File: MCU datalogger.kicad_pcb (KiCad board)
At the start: 2 copper layers, 29 parts, among them J1 Conn_01x04_Pin, J2 Conn_01x04_Pin, J3 Conn_01x09_Pin, J4 Conn_02x03_Odd_Even, U1 24LC1025, U2 24LC1025, U3 ATMEGA328P-AU, U4 DS1337S_, Y1 32.768 KHz, Y2 16MHz

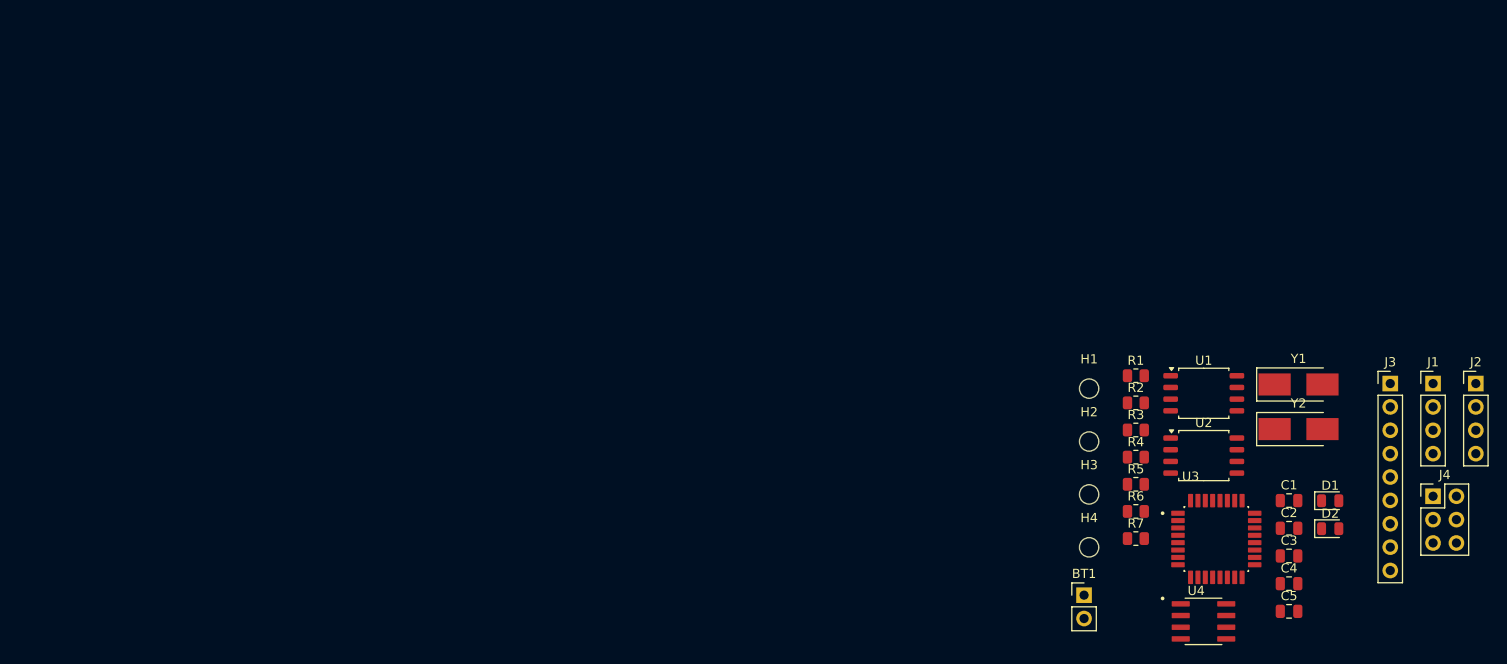
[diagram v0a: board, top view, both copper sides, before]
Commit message: complete placement of footprints
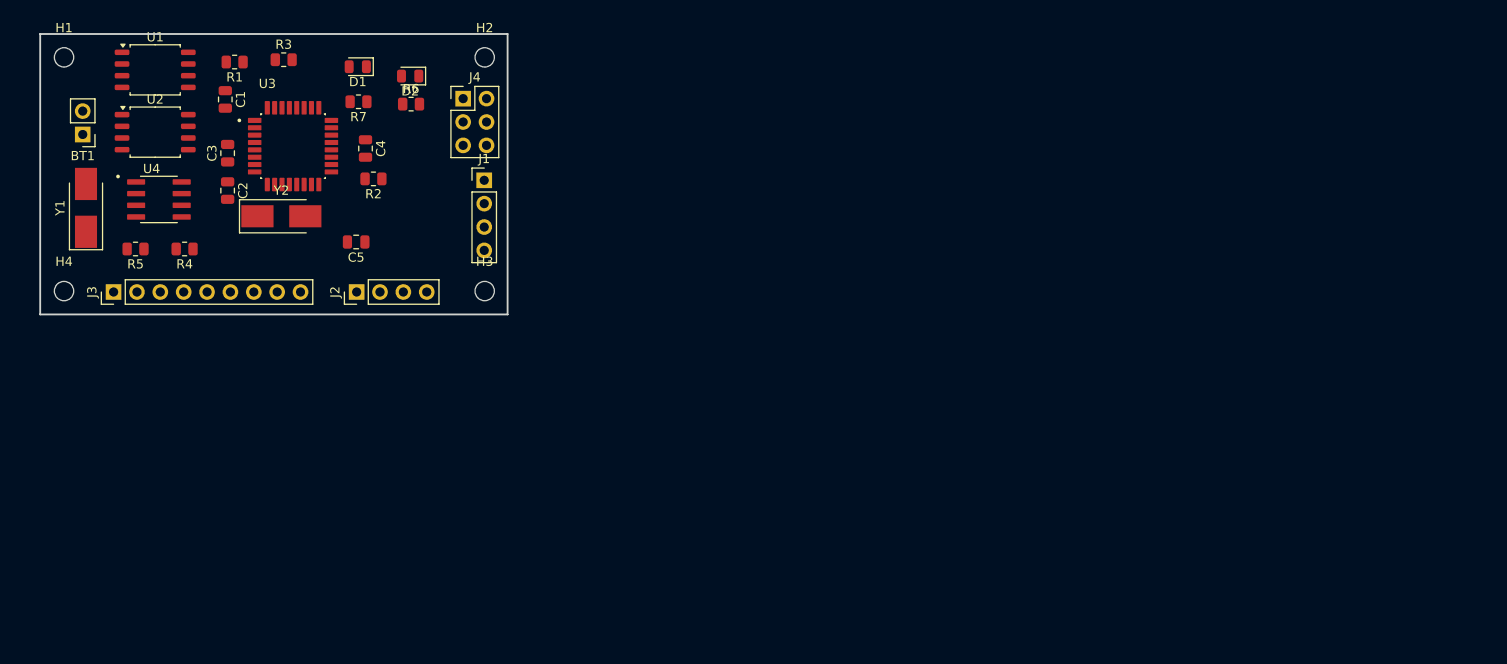
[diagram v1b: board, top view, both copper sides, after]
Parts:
- moved J3 139.1 mm to (104.4, 91.5), turned to 90 degrees
- moved Y1 133.2 mm to (101.4, 82.4), turned to 90 degrees
- moved C1 123.6 mm to (116.6, 70.6), turned to -90 degrees
- moved C3 123.4 mm to (116.8, 76.5), turned to 90 degrees
- moved U4 122.4 mm to (109.4, 81.5)
- moved J2 122.0 mm to (130.9, 91.5), turned to 90 degrees
- moved C2 121.1 mm to (116.8, 80.5), turned to -90 degrees
- moved BT1 119.8 mm to (101.1, 74.4), turned to 180 degrees
- moved U1 119.3 mm to (109.0, 67.4)
- moved U2 119.3 mm to (109.0, 74.2)
- moved H1 117.1 mm to (99.1, 66.0)
- moved D1 115.7 mm to (131.0, 67.1), turned to 180 degrees
- moved H4 114.8 mm to (99.1, 91.4)
- moved J4 113.9 mm to (142.4, 70.5)
- moved Y2 112.9 mm to (122.7, 83.3)
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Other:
- board outline added: 50.8 x 30.5 mm

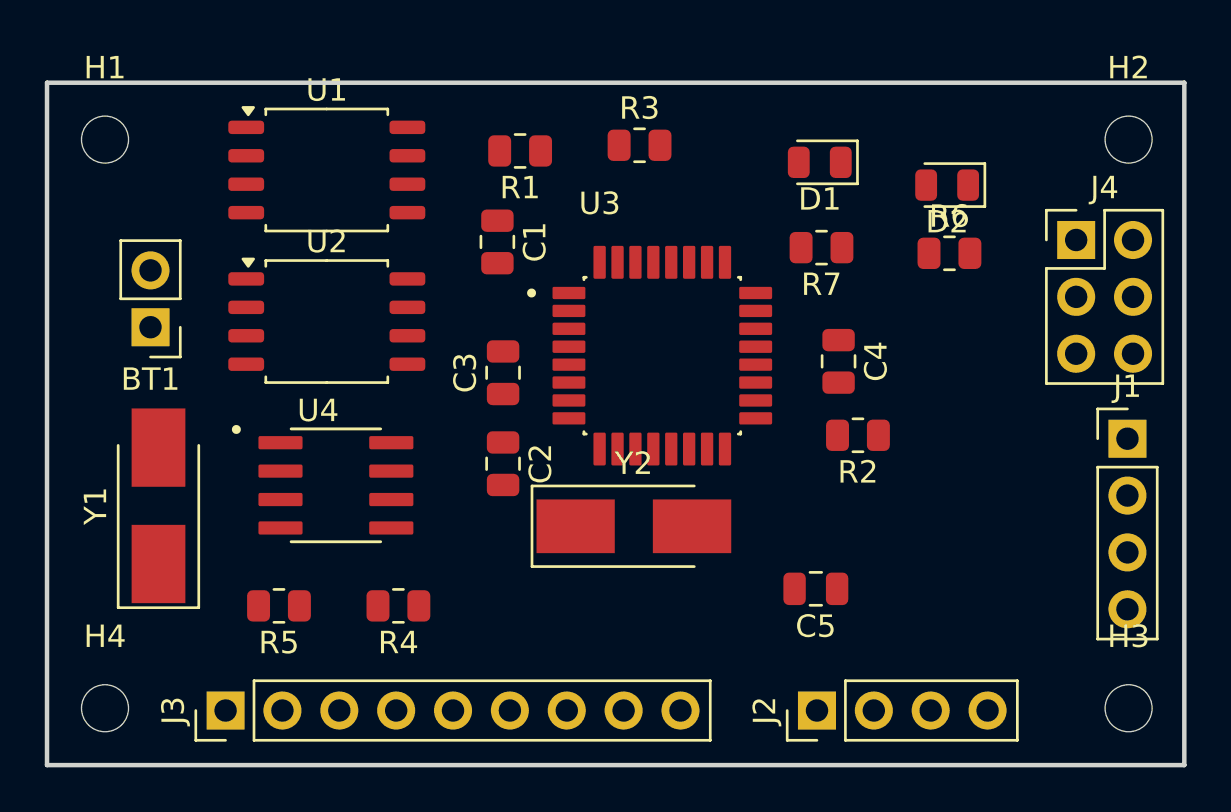
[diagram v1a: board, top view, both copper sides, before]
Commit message: routing expect gnd and vcc
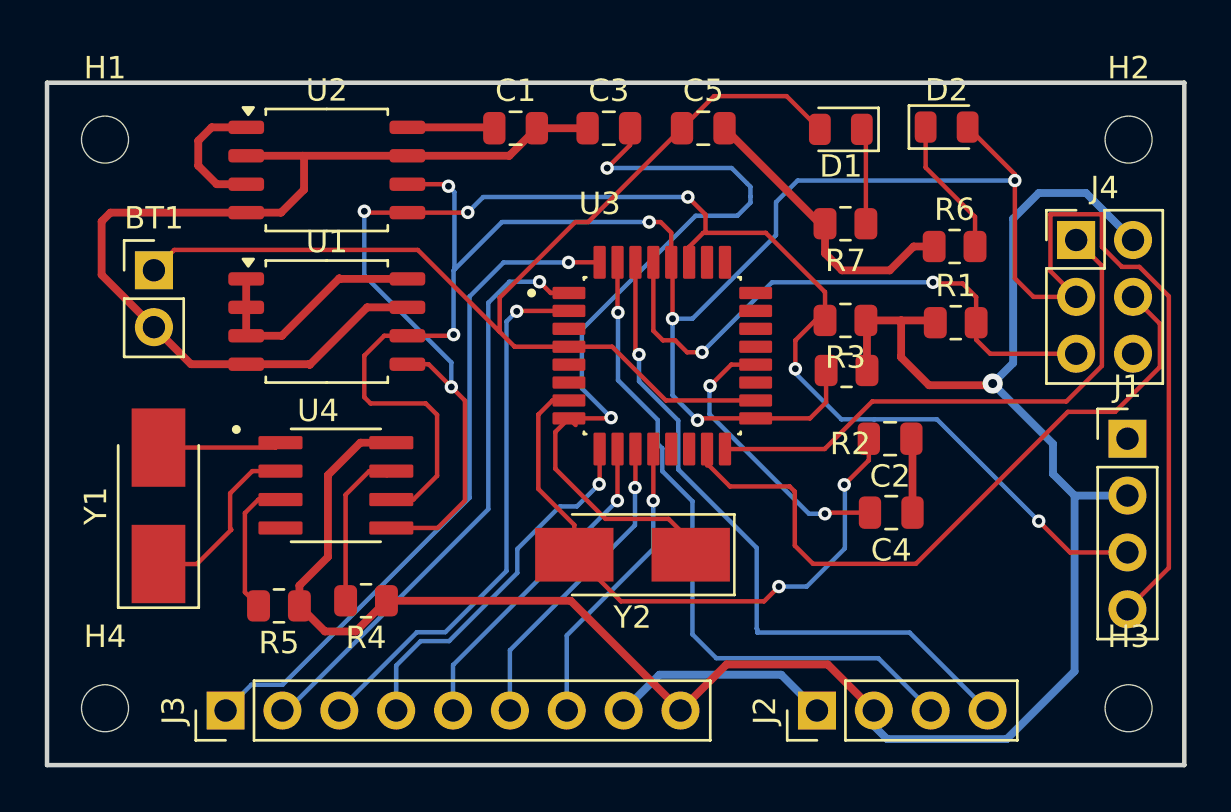
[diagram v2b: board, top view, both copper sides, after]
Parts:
- moved C5 21.2 mm to (125.8, 65.5), turned to 0 degrees
- moved R1 20.9 mm to (137.1, 74.2), turned to 0 degrees
- moved C2 17.3 mm to (134.1, 79.4), turned to 180 degrees
- moved R3 12.1 mm to (132.1, 74.1), turned to 180 degrees
- moved C3 11.9 mm to (121.6, 65.5), turned to 0 degrees
- moved C4 7.15 mm to (134.2, 82.7), turned to 180 degrees
- moved U1 6.77 mm to (109.0, 74.2)
- moved U2 6.77 mm to (109.0, 67.4)
- moved C1 5.14 mm to (117.4, 65.5), turned to 0 degrees
- moved R2 2.94 mm to (132.2, 76.4)
- moved D2 2.59 mm to (136.7, 65.5), turned to 0 degrees
- moved BT1 2.55 mm to (101.2, 71.9), turned to 0 degrees
- moved D1 1.75 mm to (131.9, 65.6)
- moved R7 1.51 mm to (132.1, 69.8)
- moved R4 1.46 mm to (110.7, 86.6)
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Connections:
- J2 pad 3: /RX -> /TX
- J2 pad 4: /TX -> /RX
- J4 pad 1: /MOSI -> /MISO
- J4 pad 4: /MISO -> /MOSI
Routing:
- net /VCC: track 0.00 -> 114.9 mm, vias 0 -> 1
- net /SCK: track 0.00 -> 106.7 mm, vias 0 -> 6
- net GND: track 0.00 -> 72.2 mm
- net /SDA: track 0.00 -> 68.4 mm, vias 0 -> 6
- net Net-(BT1-+): track 0.00 -> 50.2 mm
- net Net-(U3-PB7): track 0.00 -> 36.8 mm, vias 0 -> 2
- net /MOSI: track 0.00 -> 32.1 mm
- net /RX: track 0.00 -> 30.5 mm, vias 0 -> 1
- net /D2: track 0.00 -> 30.3 mm, vias 0 -> 1
- net /TX: track 0.00 -> 30.1 mm, vias 0 -> 1
- net Net-(U3-PB6): track 0.00 -> 27.8 mm, vias 0 -> 2
- net /D3: track 0.00 -> 26.3 mm, vias 0 -> 1
- net /RST: track 0.00 -> 26.1 mm, vias 0 -> 2
- net /MISO: track 0.00 -> 24.5 mm
- net /D4: track 0.00 -> 24.2 mm, vias 0 -> 1
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
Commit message: routing complete
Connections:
- BT1 pad 1: Net-(BT1-+) -> /VCC
- C5 pad 1: Net-(BT1-+) -> /VCC
- D1 pad 2: Net-(BT1-+) -> /VCC
- U3 pad 18: Net-(BT1-+) -> /VCC
- U3 pad 4: Net-(BT1-+) -> /VCC
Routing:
- net /VCC: track 114.9 -> 166.2 mm, vias 1 -> 3
- net Net-(BT1-+): track 50.2 -> 0.00 mm
- net GND: track 72.2 -> 114.6 mm, vias 0 -> 7
- net /MOSI: track 32.1 -> 33.1 mm
- net /SCK: track 106.7 -> 105.9 mm
- added copper zone on F.Cu, net /VCC
- added copper zone on B.Cu, net GND

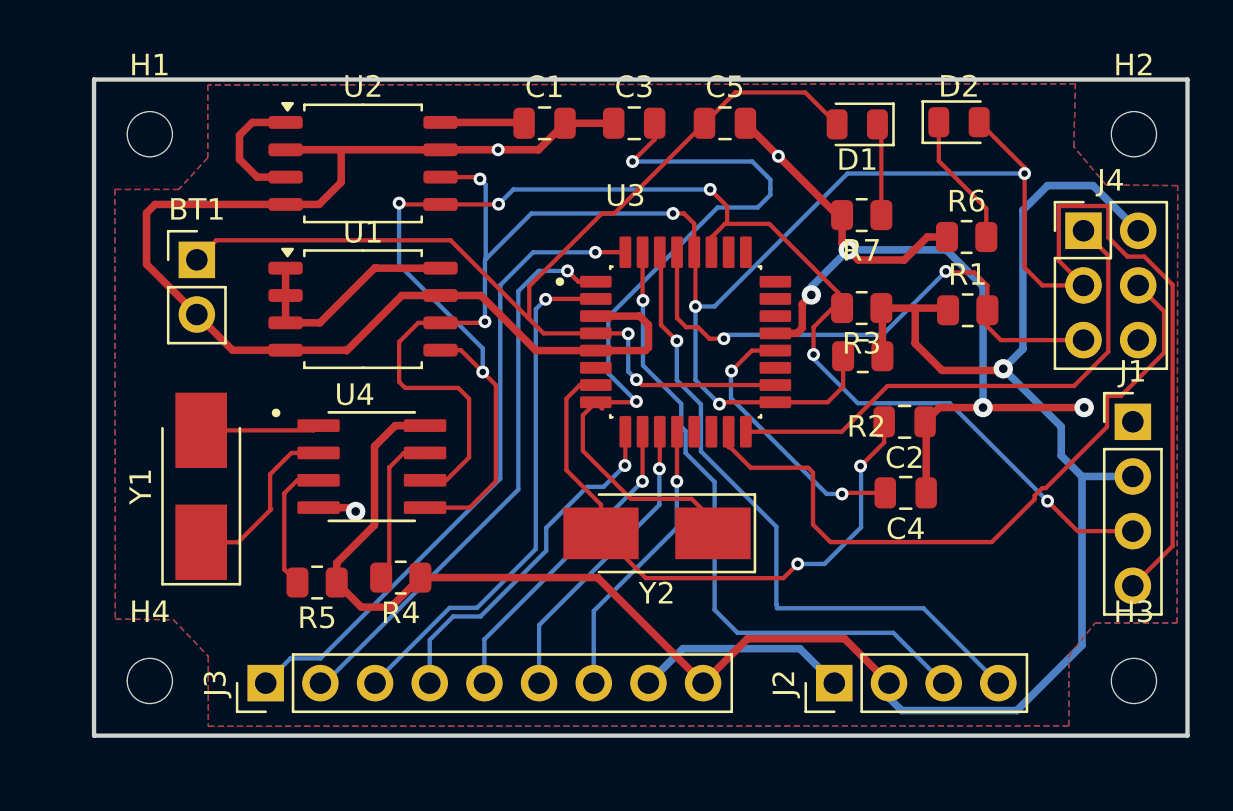
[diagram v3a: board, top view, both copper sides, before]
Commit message: fixing silkscreen
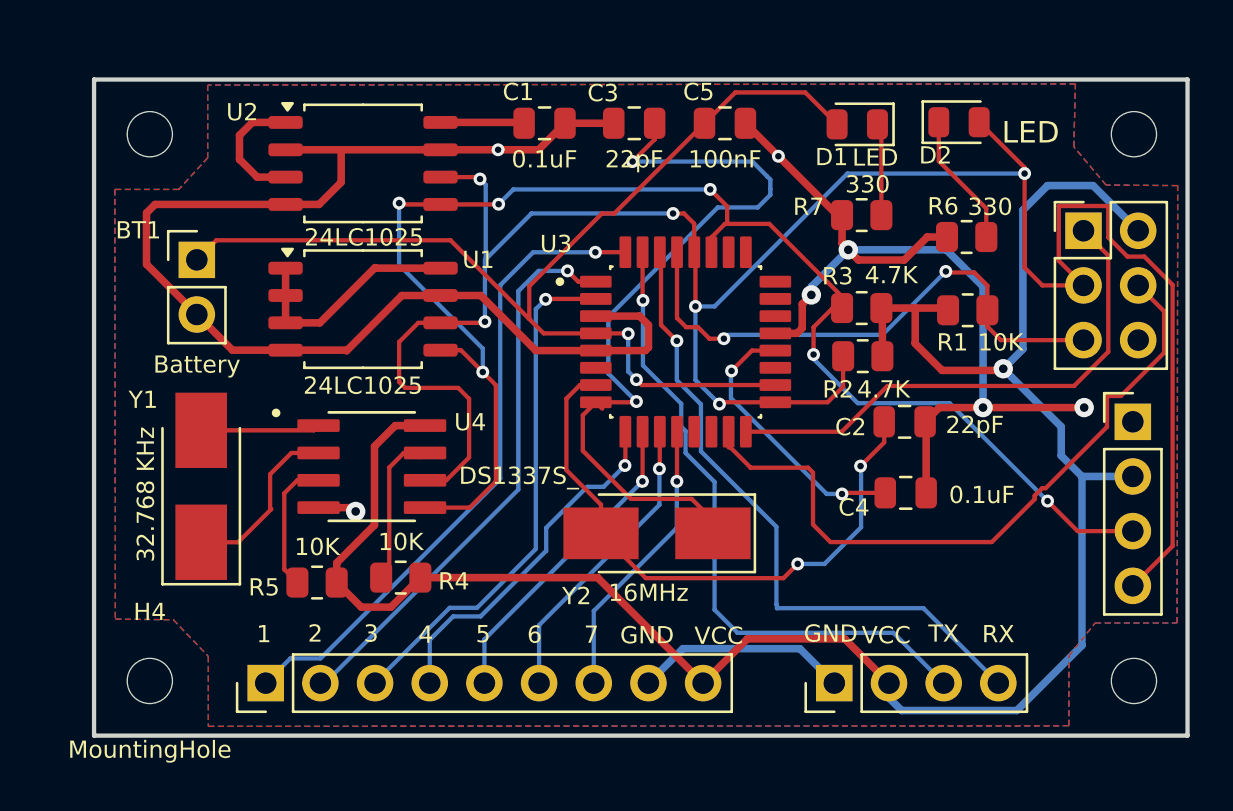
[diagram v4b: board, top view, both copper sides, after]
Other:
- board text added: "1"
- board text added: "2"
- board text added: "3"
- board text added: "4"
- board text added: "5"
- board text added: "6"
- board text added: "7"
- board text added: "GND"
- board text added: "RX"
- board text added: "TX"
- board text added: "VCC"
